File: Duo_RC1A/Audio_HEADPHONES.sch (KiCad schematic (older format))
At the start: 28 parts

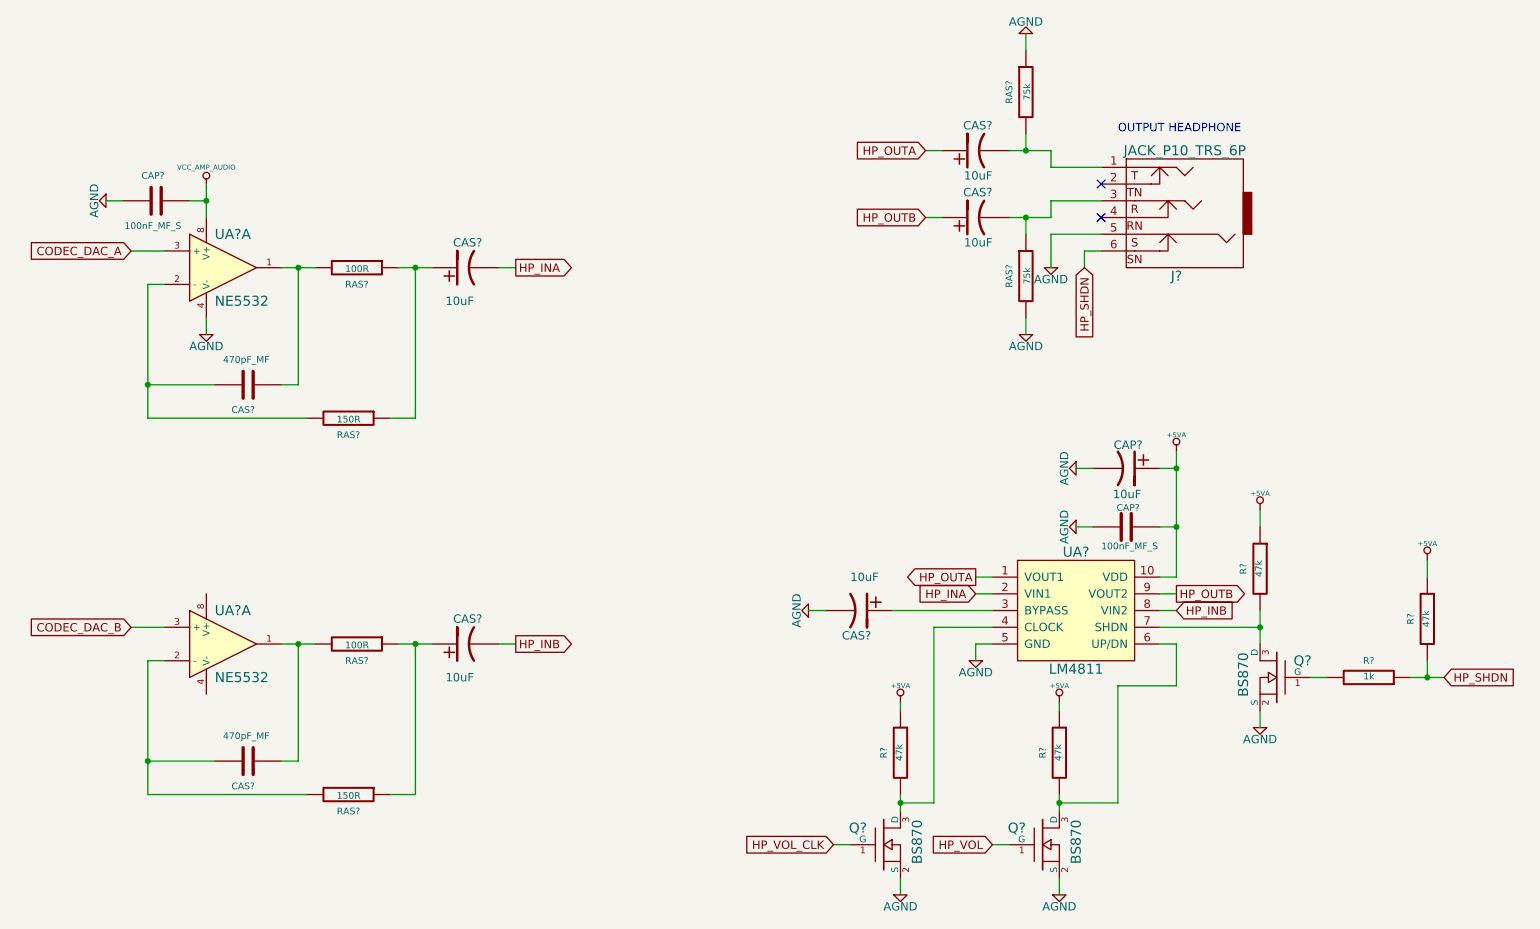
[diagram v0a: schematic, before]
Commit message: wip on issue #15: done updating the schematics for using the ICnovaA20 coreboard.
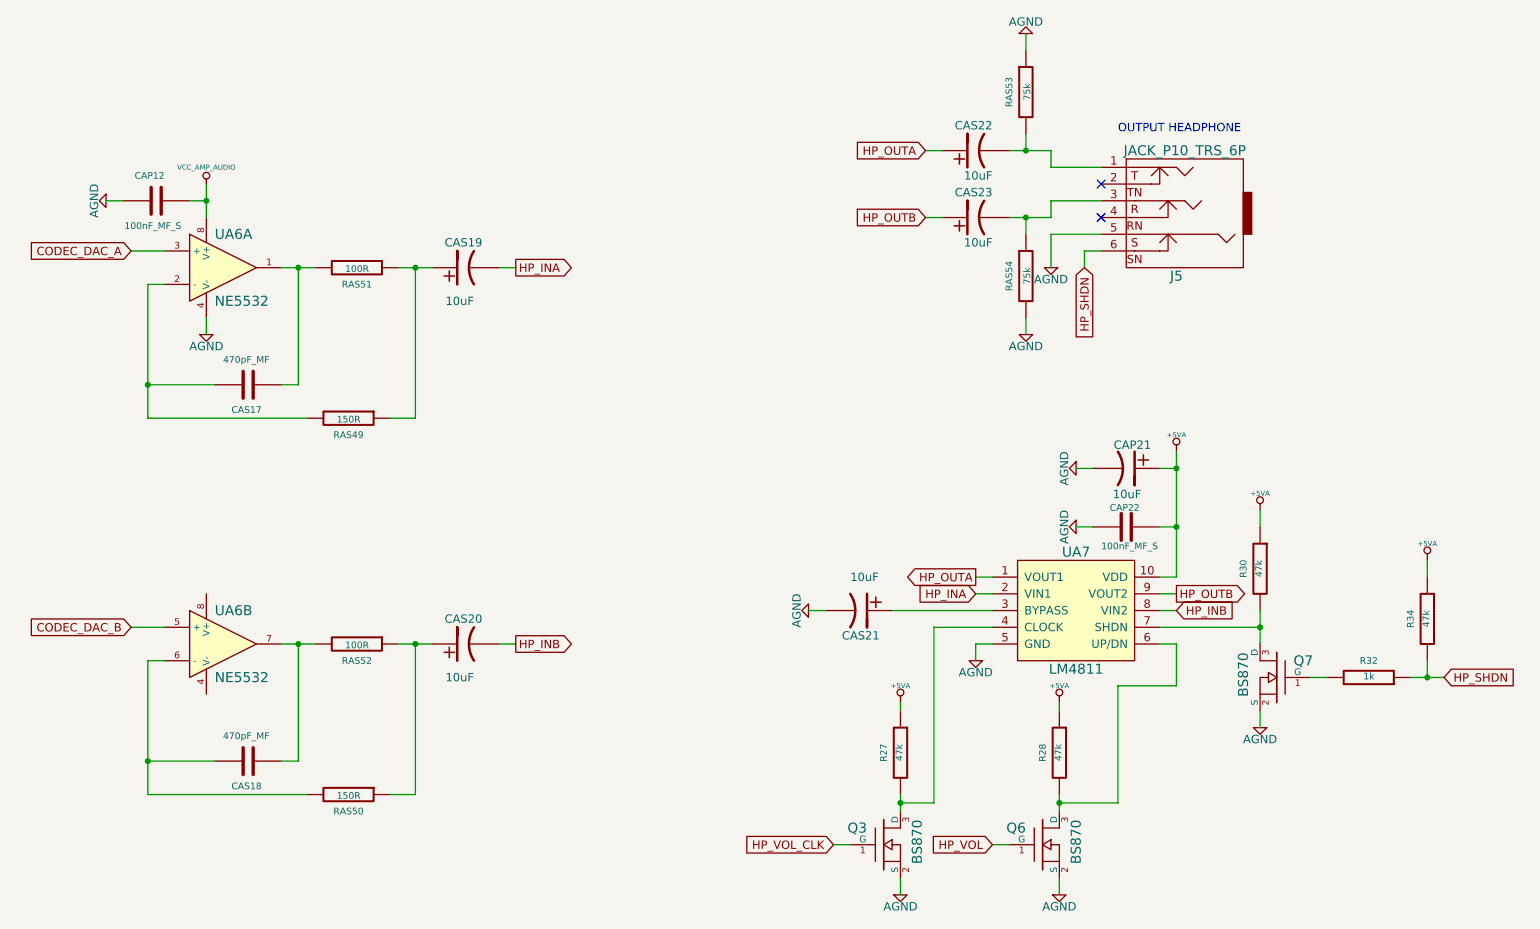
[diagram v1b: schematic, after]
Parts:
- gave numbers to parts that had none: 27
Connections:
- net CODEC_DAC_B: now also UA6.5 (+); no longer UA6.3 (+)
- net at CAS18.1, RAS52.2: now also UA6.7; no longer UA6.1
- net at CAS18.2, RAS50.2: now also UA6.6 (-); no longer UA6.2 (-)
